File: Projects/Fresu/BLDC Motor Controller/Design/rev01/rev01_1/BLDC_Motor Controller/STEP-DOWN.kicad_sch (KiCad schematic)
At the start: 10 parts, among them U4 AMS1117-3.3

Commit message: Update 13
Added:
1) USB Schematic
2) footprints to all parts
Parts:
- C55, C56, C57, C58: footprint (none) -> Capacitor_SMD:C_0603_1608Metric
- D12, D9: footprint (none) -> LED_SMD:LED_1206_3216Metric
- R50, R51: footprint (none) -> Resistor_SMD:R_0603_1608Metric_Pad0.98x0.95mm_HandSolder
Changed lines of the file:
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@@
       (effects (font (size 1.27 1.27)) (justify left))
     )
-    (property "Footprint" "" (at 160.3248 82.55 0)
+    (property "Footprint" "Capacitor_SMD:C_0603_1608Metric" (at 160.3248 82.55 0)
       (effects (font (size 1.27 1.27)) hide)
     )
@@
       (effects (font (size 1.27 1.27)) (justify right))
     )
-    (property "Footprint" "" (at 210.82 90.17 0)
+    (property "Footprint" "LED_SMD:LED_1206_3216Metric" (at 210.82 90.17 0)
       (effects (font (size 1.27 1.27)) hide)
     )
@@
       (effects (font (size 1.27 1.27)) (justify left))
     )
-    (property "Footprint" "" (at 212.598 80.01 90)
+    (property "Footprint" "Resistor_SMD:R_0603_1608Metric_Pad0.98x0.95mm_HandSolder" (at 212.598 80.01 90)
       (effects (font (size 1.27 1.27)) hide)
     )
@@
       (effects (font (size 1.27 1.27)) (justify left))
     )
-    (property "Footprint" "" (at 168.6052 82.55 0)
+    (property "Footprint" "Capacitor_SMD:C_0603_1608Metric" (at 168.6052 82.55 0)
       (effects (font (size 1.27 1.27)) hide)
     )
@@
       (effects (font (size 1.27 1.27)) (justify left))
     )
-    (property "Footprint" "" (at 121.6152 82.55 0)
+    (property "Footprint" "Capacitor_SMD:C_0603_1608Metric" (at 121.6152 82.55 0)
       (effects (font (size 1.27 1.27)) hide)
     )
@@
       (effects (font (size 1.27 1.27)) (justify right))
     )
-    (property "Footprint" "" (at 86.36 90.17 0)
+    (property "Footprint" "LED_SMD:LED_1206_3216Metric" (at 86.36 90.17 0)
       (effects (font (size 1.27 1.27)) hide)
     )
@@
       (effects (font (size 1.27 1.27)) (justify left))
     )
-    (property "Footprint" "" (at 113.3348 82.55 0)
+    (property "Footprint" "Capacitor_SMD:C_0603_1608Metric" (at 113.3348 82.55 0)
       (effects (font (size 1.27 1.27)) hide)
     )
@@
       (effects (font (size 1.27 1.27)) (justify left))
     )
-    (property "Footprint" "" (at 84.582 80.01 90)
-      (effects (font (size 1.27 1.27)) hide)
-    )
+    (property "Footprint" "Resistor_SMD:R_0603_1608Metric_Pad0.98x0.95mm_HandSolder" (at 84.582 80.01 90)
+      (effects (font (size 1.27 1.27)) hide)
+    )

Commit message: Update 15
Fixing some schematic errors

initial layout of larger component complete
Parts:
- renumbered C56 to C59, C55 to C60, C57 to C61, C58 to C62, D9 to D12, D10 to D13, D12 to D14, R50 to R59, R51 to R60, U4 to U5
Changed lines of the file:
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@@
   (symbol (lib_id "power:GND") (at 86.36 97.79 0) (unit 1)
     (in_bom yes) (on_board yes) (dnp no) (fields_autoplaced)
-    (property "Reference" "#PWR080" (at 86.36 104.14 0)
+    (property "Reference" "#PWR093" (at 86.36 104.14 0)
       (effects (font (size 1.27 1.27)) hide)
     )
@@
       (project "BLDC_Motor Controller"
         (path "/e63e39d7-6ac0-4ffd-8aa3-1841a4541b55/ba85aeeb-1956-4c49-a97a-652e9d34f1e8"
-          (reference "#PWR080") (unit 1)
+          (reference "#PWR093") (unit 1)
         )
       )
@@
   (symbol (lib_id "power:GND") (at 139.7 85.09 0) (unit 1)
     (in_bom yes) (on_board yes) (dnp no) (fields_autoplaced)
-    (property "Reference" "#PWR078" (at 139.7 91.44 0)
+    (property "Reference" "#PWR095" (at 139.7 91.44 0)
       (effects (font (size 1.27 1.27)) hide)
     )
@@
       (project "BLDC_Motor Controller"
         (path "/e63e39d7-6ac0-4ffd-8aa3-1841a4541b55/ba85aeeb-1956-4c49-a97a-652e9d34f1e8"
-          (reference "#PWR078") (unit 1)
+          (reference "#PWR095") (unit 1)
         )
       )
@@
   (symbol (lib_id "Device:C") (at 161.29 78.74 0) (mirror y) (unit 1)
     (in_bom yes) (on_board yes) (dnp no)
-    (property "Reference" "C57" (at 157.48 77.47 0)
+    (property "Reference" "C61" (at 157.48 77.47 0)
       (effects (font (size 1.27 1.27)) (justify left))
     )
@@
       (project "BLDC_Motor Controller"
         (path "/e63e39d7-6ac0-4ffd-8aa3-1841a4541b55/ba85aeeb-1956-4c49-a97a-652e9d34f1e8"
-          (reference "C57") (unit 1)
+          (reference "C61") (unit 1)
         )
       )
@@
   (symbol (lib_id "Device:LED") (at 210.82 90.17 270) (mirror x) (unit 1)
     (in_bom yes) (on_board yes) (dnp no) (fields_autoplaced)
-    (property "Reference" "D12" (at 207.01 90.4875 90)
+    (property "Reference" "D14" (at 207.01 90.4875 90)
       (effects (font (size 1.27 1.27)) (justify right))
     )
@@
       (project "BLDC_Motor Controller"
         (path "/e63e39d7-6ac0-4ffd-8aa3-1841a4541b55/ba85aeeb-1956-4c49-a97a-652e9d34f1e8"
-          (reference "D12") (unit 1)
+          (reference "D14") (unit 1)
         )
       )
@@
   (symbol (lib_id "Device:R") (at 210.82 80.01 0) (mirror y) (unit 1)
     (in_bom yes) (on_board yes) (dnp no) (fields_autoplaced)
-    (property "Reference" "R51" (at 208.28 78.74 0)
+    (property "Reference" "R60" (at 208.28 78.74 0)
       (effects (font (size 1.27 1.27)) (justify left))
     )
@@
       (project "BLDC_Motor Controller"
         (path "/e63e39d7-6ac0-4ffd-8aa3-1841a4541b55/ba85aeeb-1956-4c49-a97a-652e9d34f1e8"
-          (reference "R51") (unit 1)
+          (reference "R60") (unit 1)
         )
       )
@@
   (symbol (lib_id "Device:C") (at 167.64 78.74 0) (unit 1)
     (in_bom yes) (on_board yes) (dnp no) (fields_autoplaced)
-    (property "Reference" "C58" (at 171.45 77.47 0)
+    (property "Reference" "C62" (at 171.45 77.47 0)
       (effects (font (size 1.27 1.27)) (justify left))
     )
@@
       (project "BLDC_Motor Controller"
         (path "/e63e39d7-6ac0-4ffd-8aa3-1841a4541b55/ba85aeeb-1956-4c49-a97a-652e9d34f1e8"
-          (reference "C58") (unit 1)
+          (reference "C62") (unit 1)
         )
       )
@@
   (symbol (lib_id "power:+3V3") (at 210.82 66.04 0) (unit 1)
     (in_bom yes) (on_board yes) (dnp no) (fields_autoplaced)
-    (property "Reference" "#PWR082" (at 210.82 69.85 0)
+    (property "Reference" "#PWR097" (at 210.82 69.85 0)
       (effects (font (size 1.27 1.27)) hide)
     )
@@
       (project "BLDC_Motor Controller"
         (path "/e63e39d7-6ac0-4ffd-8aa3-1841a4541b55/ba85aeeb-1956-4c49-a97a-652e9d34f1e8"
-          (reference "#PWR082") (unit 1)
+          (reference "#PWR097") (unit 1)
         )
       )
@@
   (symbol (lib_id "power:GND") (at 210.82 97.79 0) (mirror y) (unit 1)
     (in_bom yes) (on_board yes) (dnp no) (fields_autoplaced)
-    (property "Reference" "#PWR083" (at 210.82 104.14 0)
+    (property "Reference" "#PWR098" (at 210.82 104.14 0)
       (effects (font (size 1.27 1.27)) hide)
     )
@@
       (project "BLDC_Motor Controller"
         (path "/e63e39d7-6ac0-4ffd-8aa3-1841a4541b55/ba85aeeb-1956-4c49-a97a-652e9d34f1e8"
-          (reference "#PWR083") (unit 1)
+          (reference "#PWR098") (unit 1)
         )
       )
@@
   (symbol (lib_id "Regulator_Linear:AMS1117-3.3") (at 139.7 74.93 0) (unit 1)
     (in_bom yes) (on_board yes) (dnp no) (fields_autoplaced)
-    (property "Reference" "U4" (at 139.7 68.58 0)
+    (property "Reference" "U5" (at 139.7 68.58 0)
       (effects (font (size 1.27 1.27)))
     )
@@
       (project "BLDC_Motor Controller"
         (path "/e63e39d7-6ac0-4ffd-8aa3-1841a4541b55/ba85aeeb-1956-4c49-a97a-652e9d34f1e8"
-          (reference "U4") (unit 1)
+          (reference "U5") (unit 1)
         )
       )
@@
   (symbol (lib_id "Device:C") (at 120.65 78.74 0) (unit 1)
     (in_bom yes) (on_board yes) (dnp no) (fields_autoplaced)
-    (property "Reference" "C55" (at 124.46 77.47 0)
+    (property "Reference" "C60" (at 124.46 77.47 0)
       (effects (font (size 1.27 1.27)) (justify left))
     )
@@
       (project "BLDC_Motor Controller"
         (path "/e63e39d7-6ac0-4ffd-8aa3-1841a4541b55/ba85aeeb-1956-4c49-a97a-652e9d34f1e8"
-          (reference "C55") (unit 1)
+          (reference "C60") (unit 1)
         )
       )
@@
   (symbol (lib_id "power:GND") (at 165.1 85.09 0) (unit 1)
     (in_bom yes) (on_board yes) (dnp no) (fields_autoplaced)
-    (property "Reference" "#PWR081" (at 165.1 91.44 0)
+    (property "Reference" "#PWR096" (at 165.1 91.44 0)
       (effects (font (size 1.27 1.27)) hide)
     )
@@
       (project "BLDC_Motor Controller"
         (path "/e63e39d7-6ac0-4ffd-8aa3-1841a4541b55/ba85aeeb-1956-4c49-a97a-652e9d34f1e8"
-          (reference "#PWR081") (unit 1)
+          (reference "#PWR096") (unit 1)
         )
       )
@@
   (symbol (lib_id "power:+5V") (at 86.36 66.04 0) (unit 1)
     (in_bom yes) (on_board yes) (dnp no) (fields_autoplaced)
-    (property "Reference" "#PWR079" (at 86.36 69.85 0)
+    (property "Reference" "#PWR092" (at 86.36 69.85 0)
       (effects (font (size 1.27 1.27)) hide)
     )
@@
       (project "BLDC_Motor Controller"
         (path "/e63e39d7-6ac0-4ffd-8aa3-1841a4541b55/ba85aeeb-1956-4c49-a97a-652e9d34f1e8"
-          (reference "#PWR079") (unit 1)
+          (reference "#PWR092") (unit 1)
         )
       )
@@
   (symbol (lib_id "Device:LED") (at 86.36 90.17 90) (unit 1)
     (in_bom yes) (on_board yes) (dnp no) (fields_autoplaced)
-    (property "Reference" "D9" (at 90.17 90.4875 90)
+    (property "Reference" "D12" (at 90.17 90.4875 90)
       (effects (font (size 1.27 1.27)) (justify right))
     )
@@
       (project "BLDC_Motor Controller"
         (path "/e63e39d7-6ac0-4ffd-8aa3-1841a4541b55/ba85aeeb-1956-4c49-a97a-652e9d34f1e8"
-          (reference "D9") (unit 1)
+          (reference "D12") (unit 1)
         )
       )
@@
   (symbol (lib_id "power:GND") (at 118.11 85.09 0) (unit 1)
     (in_bom yes) (on_board yes) (dnp no) (fields_autoplaced)
-    (property "Reference" "#PWR077" (at 118.11 91.44 0)
+    (property "Reference" "#PWR094" (at 118.11 91.44 0)
       (effects (font (size 1.27 1.27)) hide)
     )
@@
       (project "BLDC_Motor Controller"
         (path "/e63e39d7-6ac0-4ffd-8aa3-1841a4541b55/ba85aeeb-1956-4c49-a97a-652e9d34f1e8"
-          (reference "#PWR077") (unit 1)
+          (reference "#PWR094") (unit 1)
         )
       )
@@
   (symbol (lib_id "Device:C") (at 114.3 78.74 0) (mirror y) (unit 1)
     (in_bom yes) (on_board yes) (dnp no)
-    (property "Reference" "C56" (at 110.49 77.47 0)
+    (property "Reference" "C59" (at 110.49 77.47 0)
       (effects (font (size 1.27 1.27)) (justify left))
     )
@@
       (project "BLDC_Motor Controller"
         (path "/e63e39d7-6ac0-4ffd-8aa3-1841a4541b55/ba85aeeb-1956-4c49-a97a-652e9d34f1e8"
-          (reference "C56") (unit 1)
+          (reference "C59") (unit 1)
         )
       )
@@
   (symbol (lib_id "Device:R") (at 86.36 80.01 0) (unit 1)
     (in_bom yes) (on_board yes) (dnp no) (fields_autoplaced)
-    (property "Reference" "R50" (at 88.9 78.74 0)
+    (property "Reference" "R59" (at 88.9 78.74 0)
       (effects (font (size 1.27 1.27)) (justify left))
     )
@@
       (project "BLDC_Motor Controller"
         (path "/e63e39d7-6ac0-4ffd-8aa3-1841a4541b55/ba85aeeb-1956-4c49-a97a-652e9d34f1e8"
-          (reference "R50") (unit 1)
+          (reference "R59") (unit 1)
         )
       )
@@
   (symbol (lib_id "Diode:BAT60A") (at 184.15 74.93 180) (unit 1)
     (in_bom yes) (on_board yes) (dnp no) (fields_autoplaced)
-    (property "Reference" "D10" (at 184.4675 68.58 0)
+    (property "Reference" "D13" (at 184.4675 68.58 0)
       (effects (font (size 1.27 1.27)))
     )
@@
       (project "BLDC_Motor Controller"
         (path "/e63e39d7-6ac0-4ffd-8aa3-1841a4541b55/ba85aeeb-1956-4c49-a97a-652e9d34f1e8"
-          (reference "D10") (unit 1)
-        )
-      )
+          (reference "D13") (unit 1)
+        )
+      )

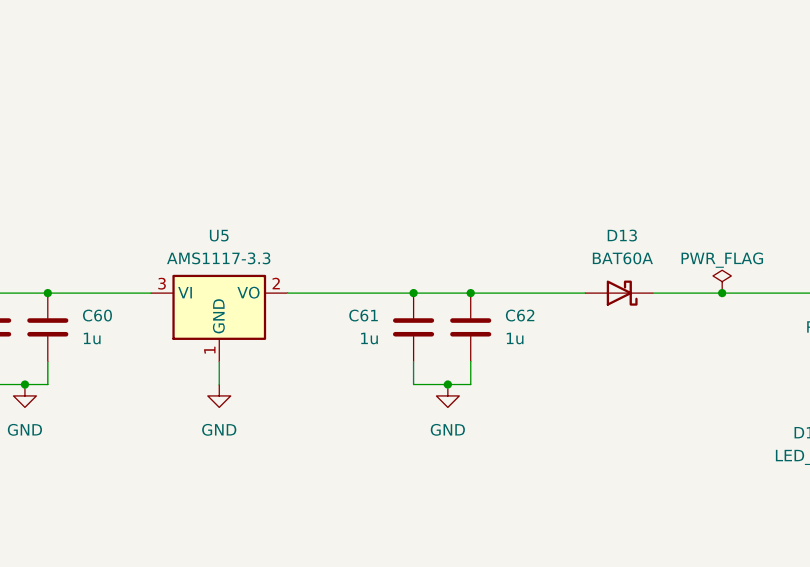
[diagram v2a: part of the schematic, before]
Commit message: Update 20
First layout completed, all tracks laid
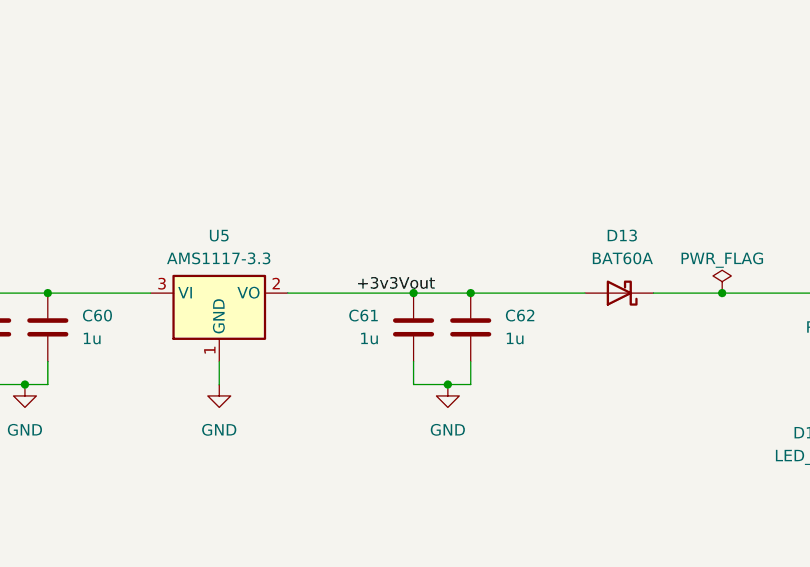
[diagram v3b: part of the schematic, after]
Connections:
- net +3v3Vout: now reaches C61.1, C62.1, D13.2 (A), U5.2 (VO)
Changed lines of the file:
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@@
     (effects (font (size 5 5) (thickness 1) bold) (justify left bottom))
+  )
+  (label "+3v3Vout" (at 154.94 74.93 0) (fields_autoplaced)
+    (effects (font (size 1.27 1.27)) (justify left bottom))
   )
   (symbol (lib_id "power:GND") (at 86.36 97.79 0) (unit 1)

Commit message: Update 26
Matched DF's Designators to mine so I can use BOM as is

Updated MFR'ing files

Rev1 Ready for release
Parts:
- renumbered C59 to C3, C60 to C4, C61 to C5, C62 to C6, D12 to D15, D13 to D3, D14 to D4, R60 to R4, R59 to R62, U5 to U1
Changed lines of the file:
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@@
 		(on_board yes)
 		(dnp no)
-		(property "Reference" "C61"
+		(property "Reference" "C5"
 			(at 157.48 77.47 0)
 			(effects
@@
 			(project "BLDC_Motor Controller"
 				(path "/e63e39d7-6ac0-4ffd-8aa3-1841a4541b55/ba85aeeb-1956-4c49-a97a-652e9d34f1e8"
-					(reference "C61")
+					(reference "C5")
 					(unit 1)
 				)
@@
 		(dnp no)
 		(fields_autoplaced yes)
-		(property "Reference" "D14"
-			(at 207.01 90.4875 90)
-			(effects
-				(font
-					(size 1.27 1.27)
-				)
-				(justify right)
+		(property "Reference" "D4"
+			(at 213.36 90.4874 90)
+			(effects
+				(font
+					(size 1.27 1.27)
+				)
+				(justify left)
 			)
 		)
 		(property "Value" "LED_G"
-			(at 207.01 93.0275 90)
-			(effects
-				(font
-					(size 1.27 1.27)
-				)
-				(justify right)
+			(at 213.36 93.0274 90)
+			(effects
+				(font
+					(size 1.27 1.27)
+				)
+				(justify left)
 			)
 		)
@@
 			(project "BLDC_Motor Controller"
 				(path "/e63e39d7-6ac0-4ffd-8aa3-1841a4541b55/ba85aeeb-1956-4c49-a97a-652e9d34f1e8"
-					(reference "D14")
+					(reference "D4")
 					(unit 1)
 				)
@@
 		(dnp no)
 		(fields_autoplaced yes)
-		(property "Reference" "R60"
-			(at 208.28 78.74 0)
-			(effects
-				(font
-					(size 1.27 1.27)
-				)
-				(justify left)
+		(property "Reference" "R4"
+			(at 213.36 78.7399 0)
+			(effects
+				(font
+					(size 1.27 1.27)
+				)
+				(justify right)
 			)
 		)
 		(property "Value" "1k"
-			(at 208.28 81.28 0)
-			(effects
-				(font
-					(size 1.27 1.27)
-				)
-				(justify left)
+			(at 213.36 81.2799 0)
+			(effects
+				(font
+					(size 1.27 1.27)
+				)
+				(justify right)
 			)
 		)
@@
 			(project "BLDC_Motor Controller"
 				(path "/e63e39d7-6ac0-4ffd-8aa3-1841a4541b55/ba85aeeb-1956-4c49-a97a-652e9d34f1e8"
-					(reference "R60")
+					(reference "R4")
 					(unit 1)
 				)
@@
 		(dnp no)
 		(fields_autoplaced yes)
-		(property "Reference" "C62"
-			(at 171.45 77.47 0)
+		(property "Reference" "C6"
+			(at 171.45 77.4699 0)
 			(effects
 				(font
@@
 		)
 		(property "Value" "1u"
-			(at 171.45 80.01 0)
+			(at 171.45 80.0099 0)
 			(effects
 				(font
@@
 			(project "BLDC_Motor Controller"
 				(path "/e63e39d7-6ac0-4ffd-8aa3-1841a4541b55/ba85aeeb-1956-4c49-a97a-652e9d34f1e8"
-					(reference "C62")
+					(reference "C6")
 					(unit 1)
 				)
@@
 		(dnp no)
 		(fields_autoplaced yes)
-		(property "Reference" "U5"
+		(property "Reference" "U1"
 			(at 139.7 68.58 0)
 			(effects
@@
 			(project "BLDC_Motor Controller"
 				(path "/e63e39d7-6ac0-4ffd-8aa3-1841a4541b55/ba85aeeb-1956-4c49-a97a-652e9d34f1e8"
-					(reference "U5")
+					(reference "U1")
 					(unit 1)
 				)
@@
 		(dnp no)
 		(fields_autoplaced yes)
-		(property "Reference" "C60"
-			(at 124.46 77.47 0)
+		(property "Reference" "C4"
+			(at 124.46 77.4699 0)
 			(effects
 				(font
@@
 		)
 		(property "Value" "1u"
-			(at 124.46 80.01 0)
+			(at 124.46 80.0099 0)
 			(effects
 				(font
@@
 			(project "BLDC_Motor Controller"
 				(path "/e63e39d7-6ac0-4ffd-8aa3-1841a4541b55/ba85aeeb-1956-4c49-a97a-652e9d34f1e8"
-					(reference "C60")
+					(reference "C4")
 					(unit 1)
 				)
@@
 		(dnp no)
 		(fields_autoplaced yes)
-		(property "Reference" "D12"
-			(at 90.17 90.4875 90)
+		(property "Reference" "D15"
+			(at 90.17 90.4874 90)
 			(effects
 				(font
@@
 		)
 		(property "Value" "LED_G"
-			(at 90.17 93.0275 90)
+			(at 90.17 93.0274 90)
 			(effects
 				(font
@@
 			(project "BLDC_Motor Controller"
 				(path "/e63e39d7-6ac0-4ffd-8aa3-1841a4541b55/ba85aeeb-1956-4c49-a97a-652e9d34f1e8"
-					(reference "D12")
+					(reference "D15")
 					(unit 1)
 				)
@@
 		(on_board yes)
 		(dnp no)
-		(property "Reference" "C59"
+		(property "Reference" "C3"
 			(at 110.49 77.47 0)
 			(effects
@@
 			(project "BLDC_Motor Controller"
 				(path "/e63e39d7-6ac0-4ffd-8aa3-1841a4541b55/ba85aeeb-1956-4c49-a97a-652e9d34f1e8"
-					(reference "C59")
+					(reference "C3")
 					(unit 1)
 				)
@@
 		(dnp no)
 		(fields_autoplaced yes)
-		(property "Reference" "R59"
-			(at 88.9 78.74 0)
+		(property "Reference" "R62"
+			(at 88.9 78.7399 0)
 			(effects
 				(font
@@
 		)
 		(property "Value" "1k"
-			(at 88.9 81.28 0)
+			(at 88.9 81.2799 0)
 			(effects
 				(font
@@
 			(project "BLDC_Motor Controller"
 				(path "/e63e39d7-6ac0-4ffd-8aa3-1841a4541b55/ba85aeeb-1956-4c49-a97a-652e9d34f1e8"
-					(reference "R59")
+					(reference "R62")
 					(unit 1)
 				)
@@
 		(dnp no)
 		(fields_autoplaced yes)
-		(property "Reference" "D13"
+		(property "Reference" "D3"
 			(at 184.4675 68.58 0)
 			(effects
@@
 			(project "BLDC_Motor Controller"
 				(path "/e63e39d7-6ac0-4ffd-8aa3-1841a4541b55/ba85aeeb-1956-4c49-a97a-652e9d34f1e8"
-					(reference "D13")
-					(unit 1)
-				)
+					(reference "D3")
+					(unit 1)
+				)
